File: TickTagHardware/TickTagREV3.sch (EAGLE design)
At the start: 18 parts, among them U1 AXE610124, U6 TPS22916

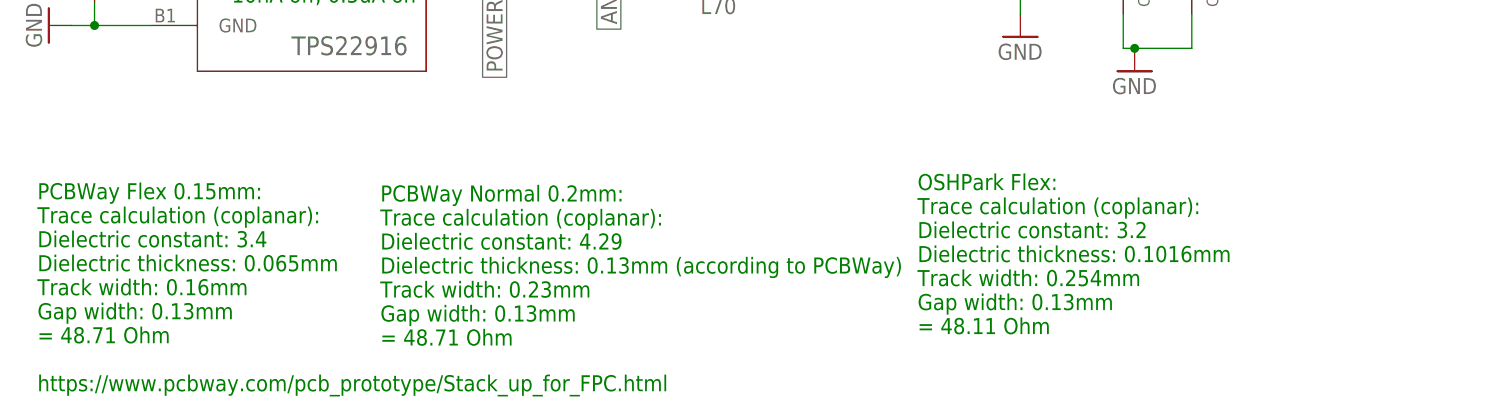
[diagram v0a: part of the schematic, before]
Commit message: added fuse writing for ATTINY1616 (alternative to 1626), removed confusing comments in schematics
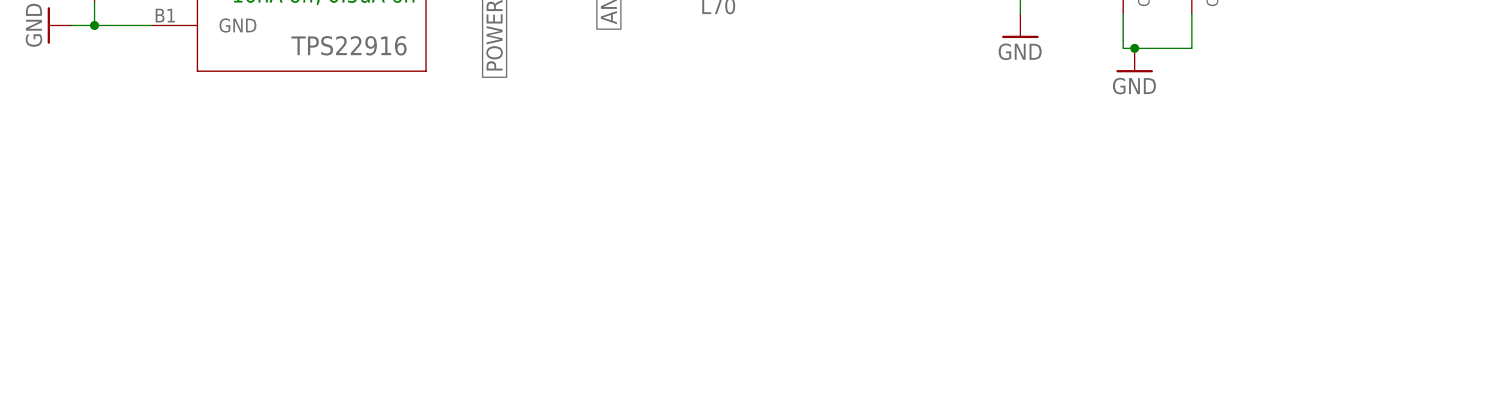
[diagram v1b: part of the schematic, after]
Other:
- note removed: "OSHPark Flex: Trace calculation (coplanar): Dielectric constant: 3.2 Dielectric thickness: 0.1016mm Track width: 0.254mm Gap width: 0.13mm = 48.11 Ohm"
- note removed: "PCBWay Flex 0.15mm: Trace calculation (coplanar): Dielectric constant: 3.4 Dielectric thickness: 0.065mm Track width: 0.16mm Gap width: 0.13mm = 48.71 Ohm https://www.pcbway.com/pcb_prototype/Stack_up_for_FPC.html"
- note removed: "PCBWay Normal 0.2mm: Trace calculation (coplanar): Dielectric constant: 4.29 Dielectric thickness: 0.13mm (according to PCBWay) Track width: 0.23mm Gap width: 0.13mm = 48.71 Ohm"
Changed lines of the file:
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@@
 <text x="-92.71" y="2.54" size="1.778" layer="91" grouprefs="LOADSWITCH">TPS22916CN
 10nA off, 0.5uA on</text>
-<text x="-16.51" y="-34.29" size="1.778" layer="91">OSHPark Flex:
-Trace calculation (coplanar):
-Dielectric constant: 3.2
-Dielectric thickness: 0.1016mm
-Track width: 0.254mm
-Gap width: 0.13mm
-= 48.11 Ohm</text>
-<text x="-114.3" y="-40.64" size="1.778" layer="91">PCBWay Flex 0.15mm:
-Trace calculation (coplanar):
-Dielectric constant: 3.4
-Dielectric thickness: 0.065mm
-Track width: 0.16mm
-Gap width: 0.13mm
-= 48.71 Ohm
-https://www.pcbway.com/pcb_prototype/Stack_up_for_FPC.html</text>
-<text x="-76.2" y="-35.56" size="1.778" layer="91">PCBWay Normal 0.2mm:
-Trace calculation (coplanar):
-Dielectric constant: 4.29
-Dielectric thickness: 0.13mm (according to PCBWay)
-Track width: 0.23mm
-Gap width: 0.13mm
-= 48.71 Ohm</text>
 </plain>
 <instances>
